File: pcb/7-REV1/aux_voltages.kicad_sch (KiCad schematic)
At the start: 11 parts, among them U18 74LVC2G14

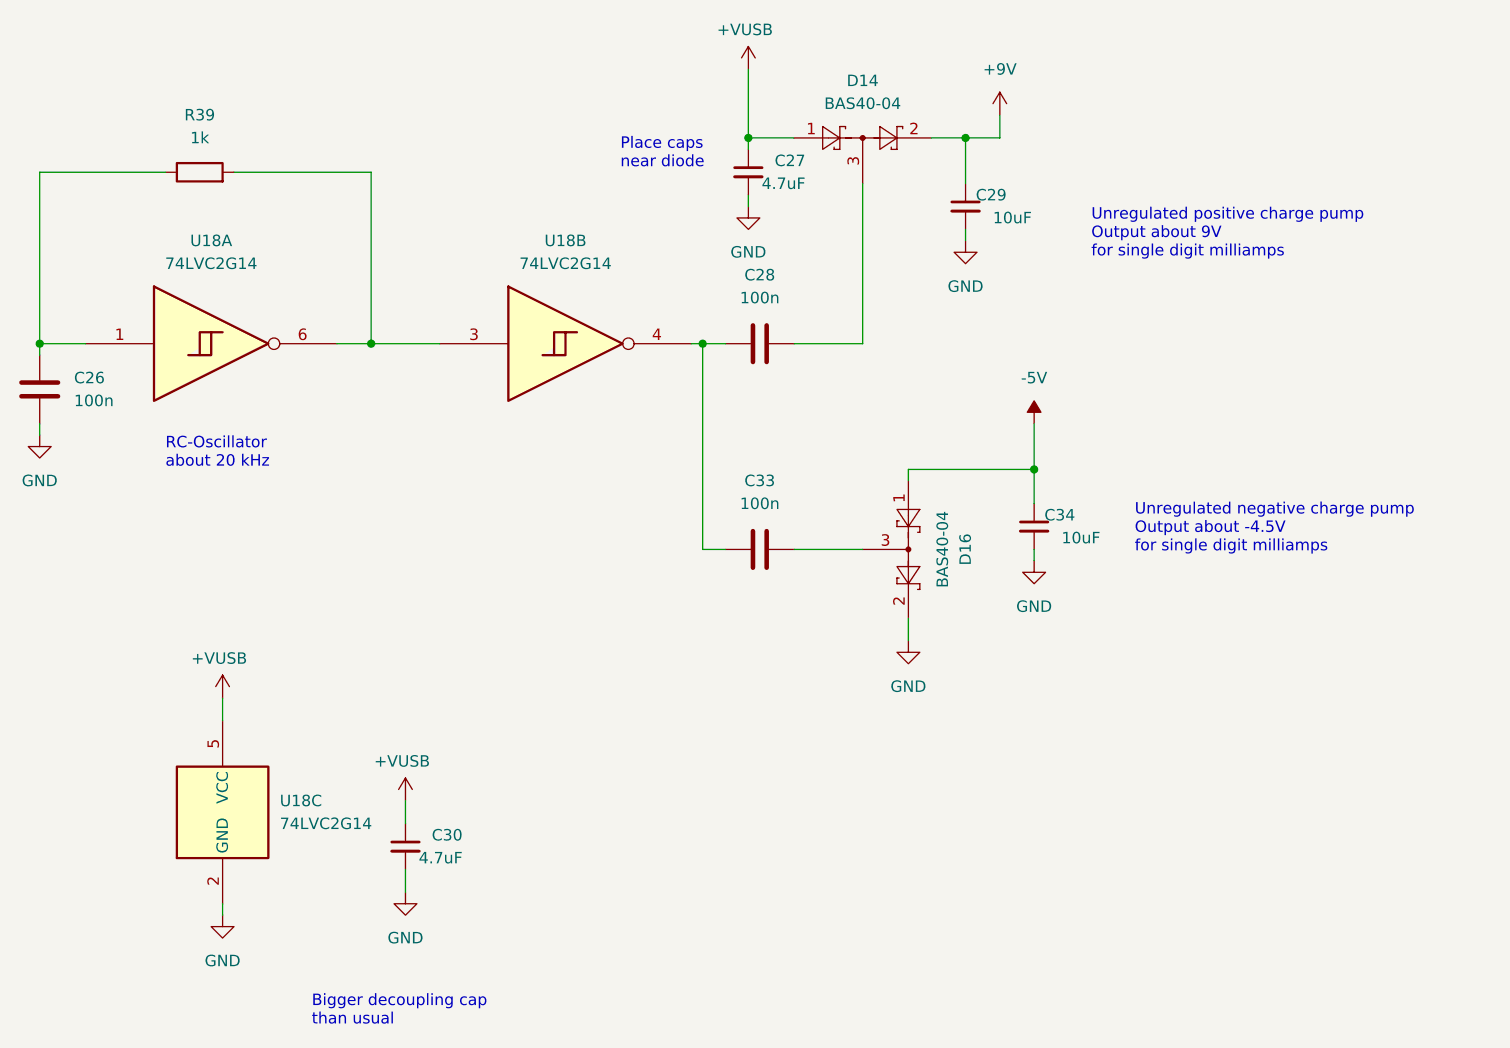
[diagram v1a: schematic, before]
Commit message: update aux voltage creation
- 100pF/200k RC oscillator for reduced current consumption
- set footprints to 0402, use default symbols that are used in other parts of the schematics
- use 4.7µF / 0402 cap for -5V:
  I guess we can get by with this as we don't have that much bias, so the cap loss should be ok
- use 10µF / 0805 for 9V:
  Too high voltage for a smaller part, voltage biassing would kill nearly all capacitance
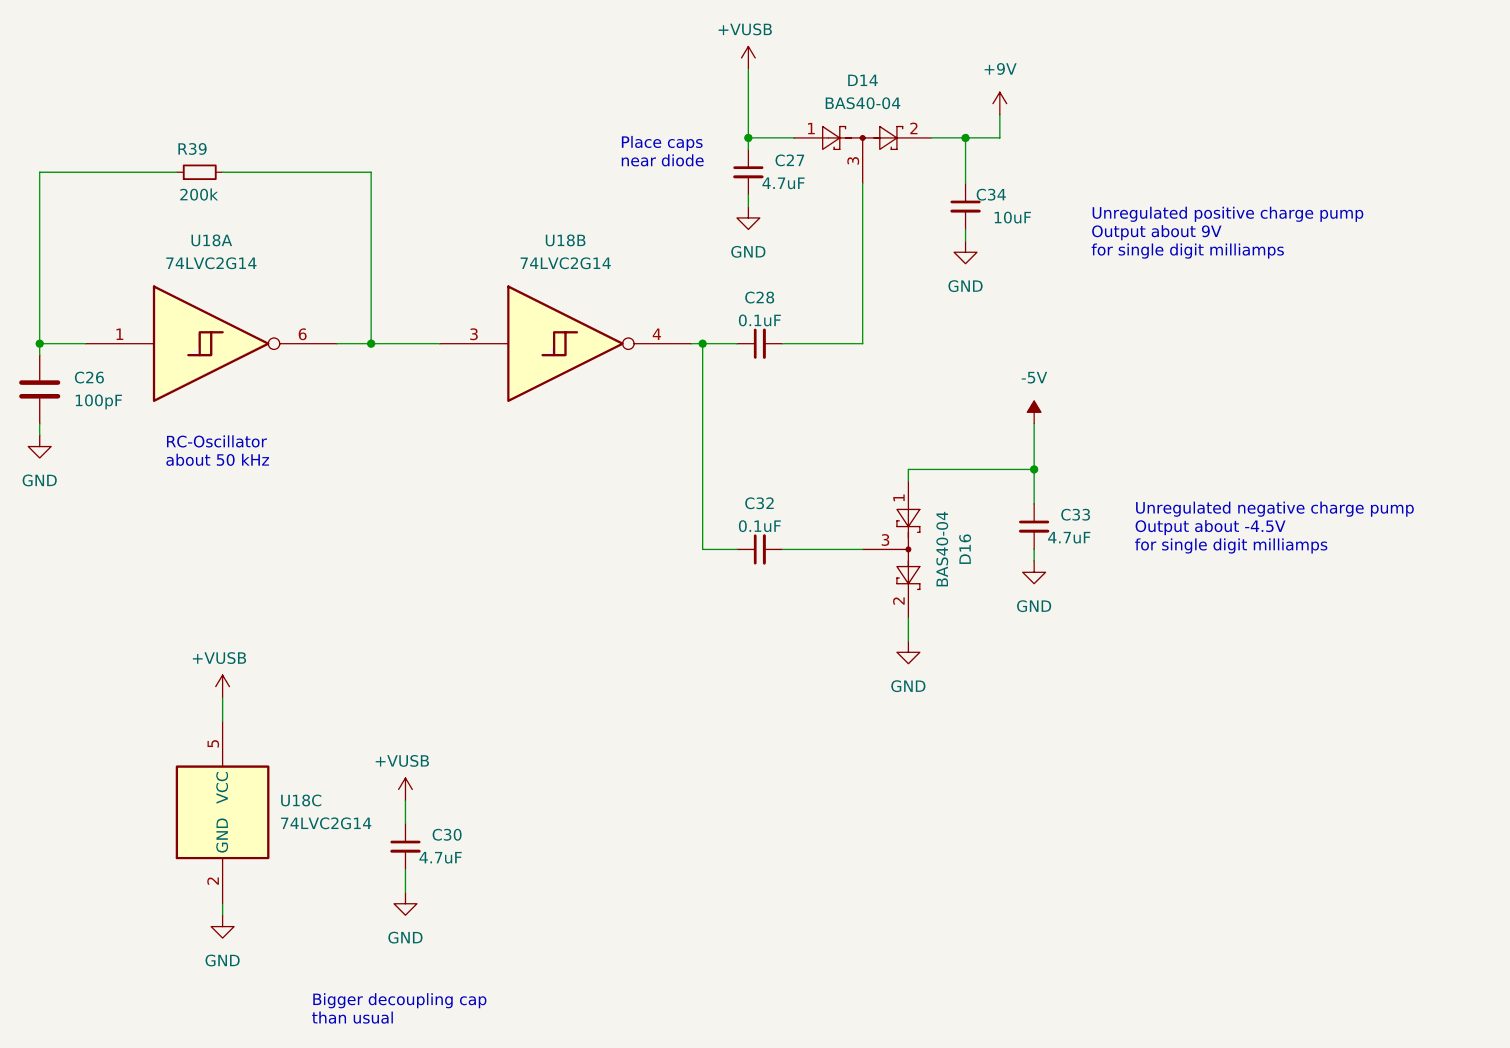
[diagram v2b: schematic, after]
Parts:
- removed C28, C33: 100n, symbol Device:C
- removed C29: 10uF, Capacitor_SMD:C_0805_2012Metric, symbol Device:C_Small
- removed R39: 1k, symbol Device:R
- added C28, C32: 0.1uF, Capacitor_SMD:C_0402_1005Metric, symbol Device:C_Small
- added C33: 4.7uF, Capacitor_SMD:C_0402_1005Metric, symbol Device:C_Small
- added R39: 200k, Resistor_SMD:R_0402_1005Metric, symbol Device:R_Small
- C26: value 100n -> 100pF; footprint (none) -> Capacitor_SMD:C_0402_1005Metric
- U18: footprint (none) -> Package_TO_SOT_SMD:SOT-363_SC-70-6
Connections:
- net +9V: now also C34.1
- net -5V: now also C33.1; no longer C34.1
- net GND: now also C33.2
- net at C26.1, U18.1: now also R39.1
- net at U18.3, U18.6: now also R39.2
- net at U18.4: now also C28.1, C32.1
- net at D14.3: now also C28.2
- net at D16.3: now also C32.2
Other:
- note added: "RC-Oscillator about 50 kHz"
- note removed: "RC-Oscillator about 20 kHz"

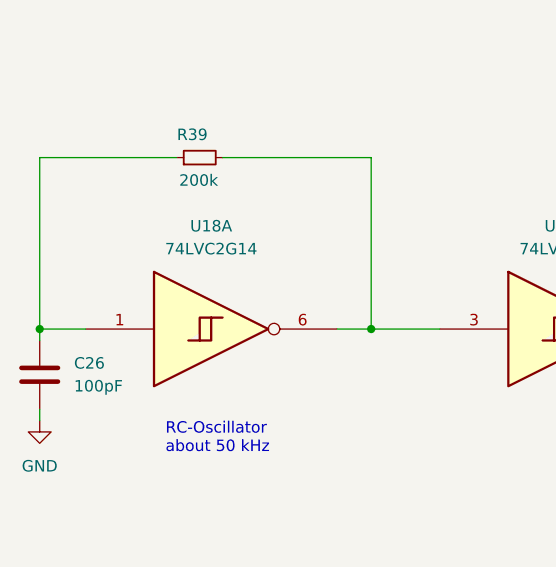
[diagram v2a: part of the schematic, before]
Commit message: reduce BOM lines by changing the Vaux oscillator to 120pF || 180k
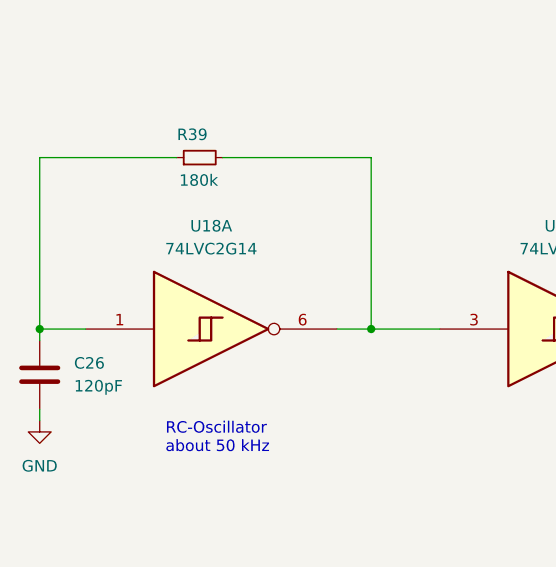
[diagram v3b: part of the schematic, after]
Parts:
- C26: value 100pF -> 120pF
- R39: value 200k -> 180k
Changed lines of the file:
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@@
 			)
 		)
-		(property "Value" "100pF"
+		(property "Value" "120pF"
 			(at 78.74 106.6799 0)
 			(effects
@@
 			)
 		)
-		(property "Value" "200k"
+		(property "Value" "180k"
 			(at 90.424 83.82 90)
 			(effects

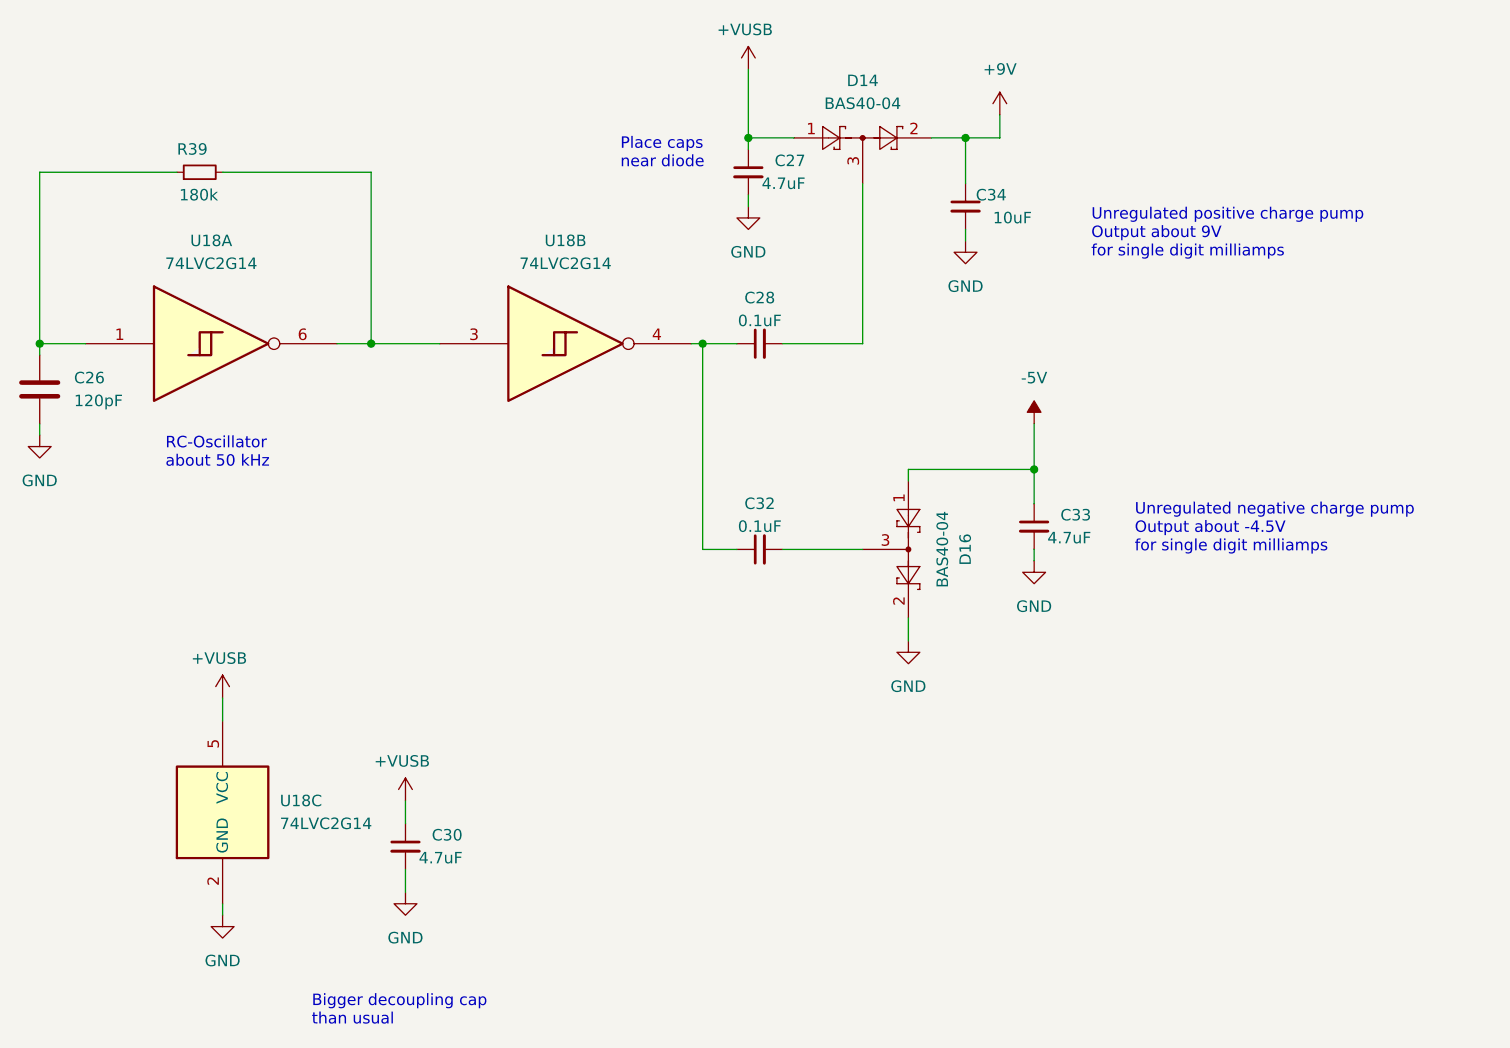
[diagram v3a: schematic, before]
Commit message: BP7REV1 2.2uF, 4.7uF-> 10uF/6.3V CL05A106MQ5NUN. 520K->470K on reset/bootloader switch.
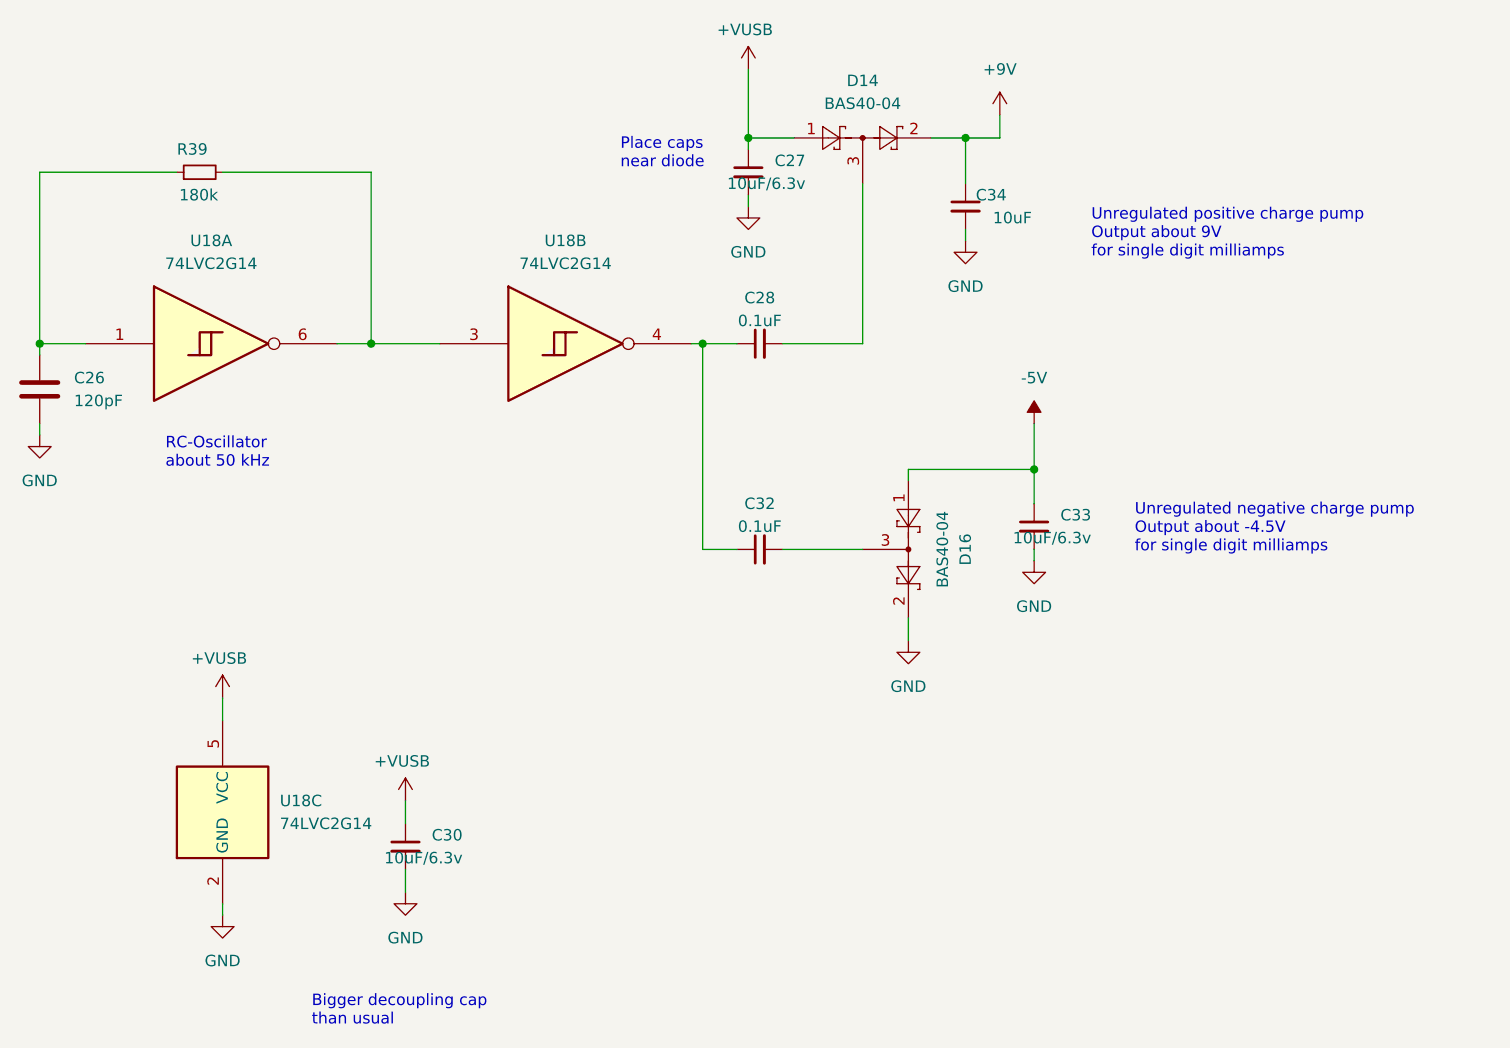
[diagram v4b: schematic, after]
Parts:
- C27, C30, C33: value 4.7uF -> 10uF/6.3v
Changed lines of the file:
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@@
 			)
 		)
-		(property "Value" "4.7uF"
+		(property "Value" "10uF/6.3v"
 			(at 121.92 157.48 0)
 			(effects
@@
 			)
 		)
-		(property "Description" ""
+		(property "Description" "CL05A106MQ5NUN"
 			(at 115.57 156.21 0)
 			(effects
@@
 			)
 		)
-		(property "Value" "4.7uF"
+		(property "Value" "10uF/6.3v"
 			(at 191.77 121.92 0)
 			(effects
@@
 			)
 		)
-		(property "Description" ""
+		(property "Description" "CL05A106MQ5NUN"
 			(at 185.42 120.65 0)
 			(effects
@@
 			)
 		)
-		(property "Value" "4.7uF"
+		(property "Value" "10uF/6.3v"
 			(at 160.02 82.55 0)
 			(effects
@@
 			)
 		)
-		(property "Description" ""
+		(property "Description" "CL05A106MQ5NUN"
 			(at 153.67 81.28 0)
 			(effects

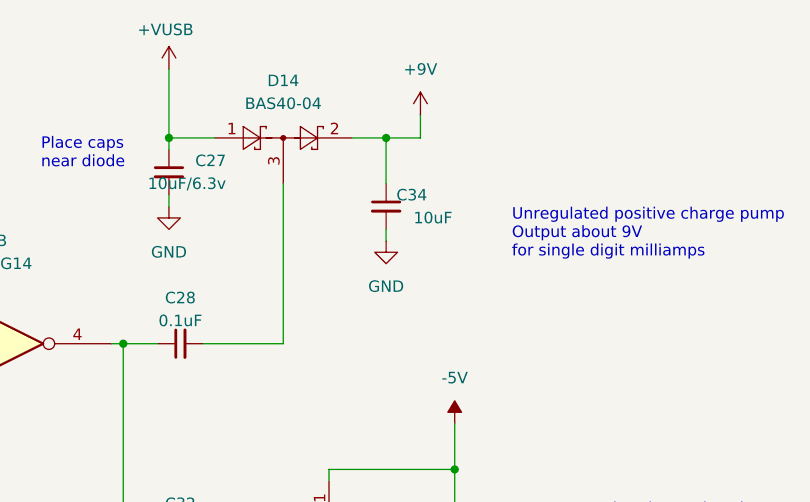
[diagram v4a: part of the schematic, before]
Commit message: specify part numbers and manufacturers in more detail - 10µF / 0805 caps - 2N7002KT fets
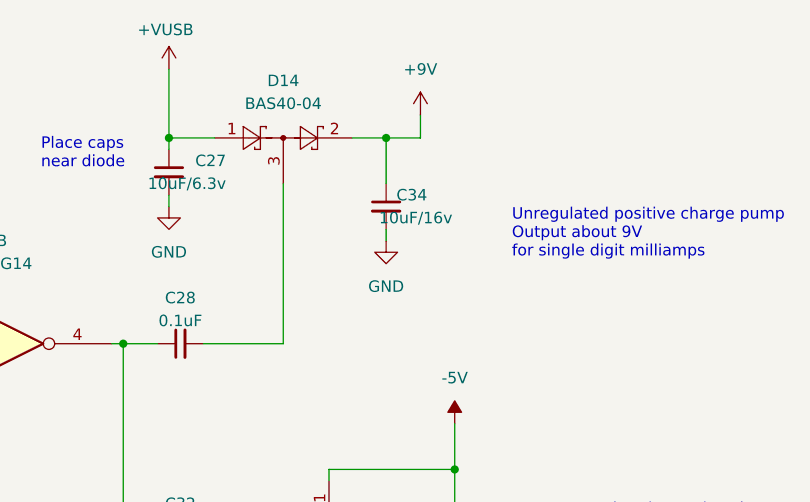
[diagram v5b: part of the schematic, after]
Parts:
- C27, C30, C33: MANUFACTURER (none) -> Samsung
- C34: value 10uF -> 10uF/16v; MANUFACTURER (none) -> Samsung
